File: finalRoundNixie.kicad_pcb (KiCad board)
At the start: 2 copper layers, 37 x 56.3 mm, 60 parts, among them J1 Conn_01x06_Male, J2 HV_IN, J3 Conn_01x06_Female, J4 HV_OUT, Q1 MMBTA42LT1, Q10 MMBTA42LT1, Q11 AO3400, Q12 AO3400, Q13 AO3400, Q14 MMBTA42LT1, Q15 MMBTA42LT1, Q2 MMBTA42LT1, Q3 MMBTA42LT1, Q4 MMBTA42LT1, Q5 MMBTA42LT1, Q6 MMBTA42LT1, Q7 MMBTA42LT1, Q8 MMBTA42LT1, Q9 MMBTA42LT1, U1 74HC595D, U2 nixie-tube-qs27, U3 74HC595D, U4 ams1117-5.0

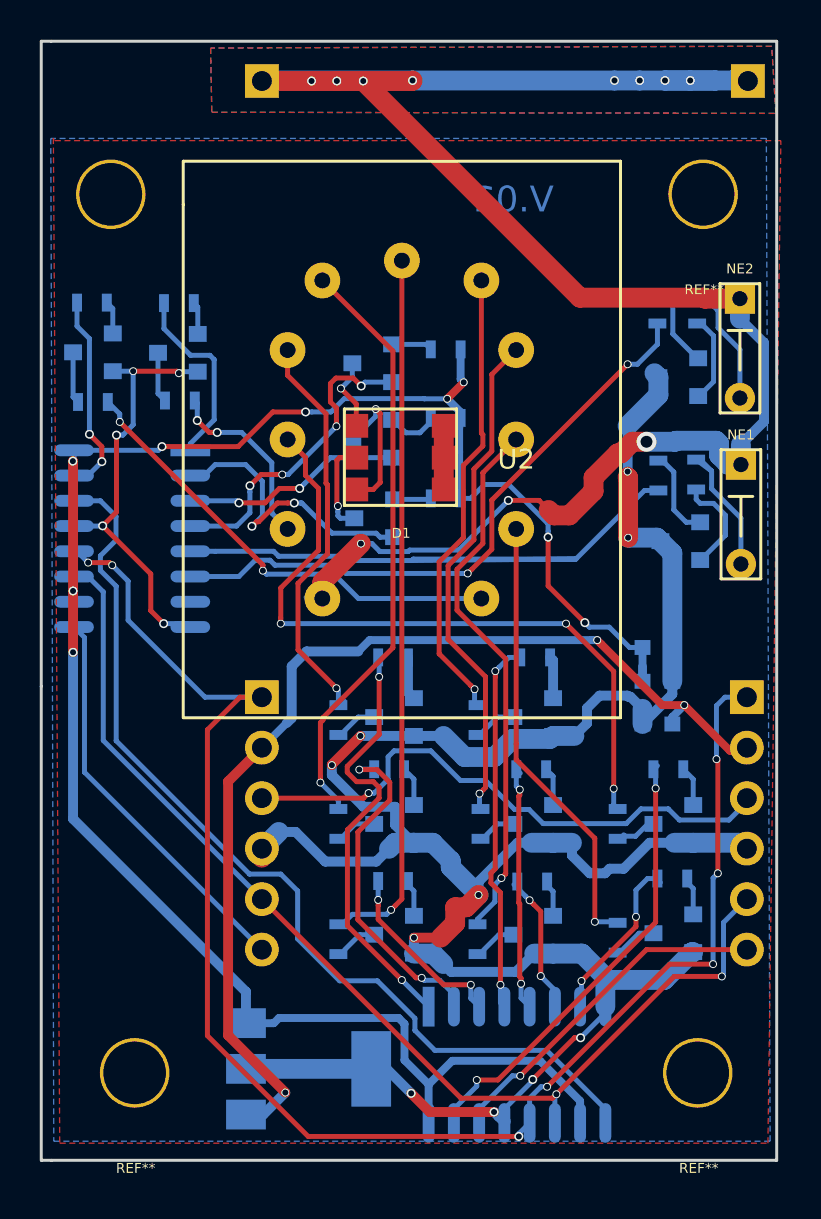
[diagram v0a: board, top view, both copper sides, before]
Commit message: routed qs27-1 on the main pcbnew
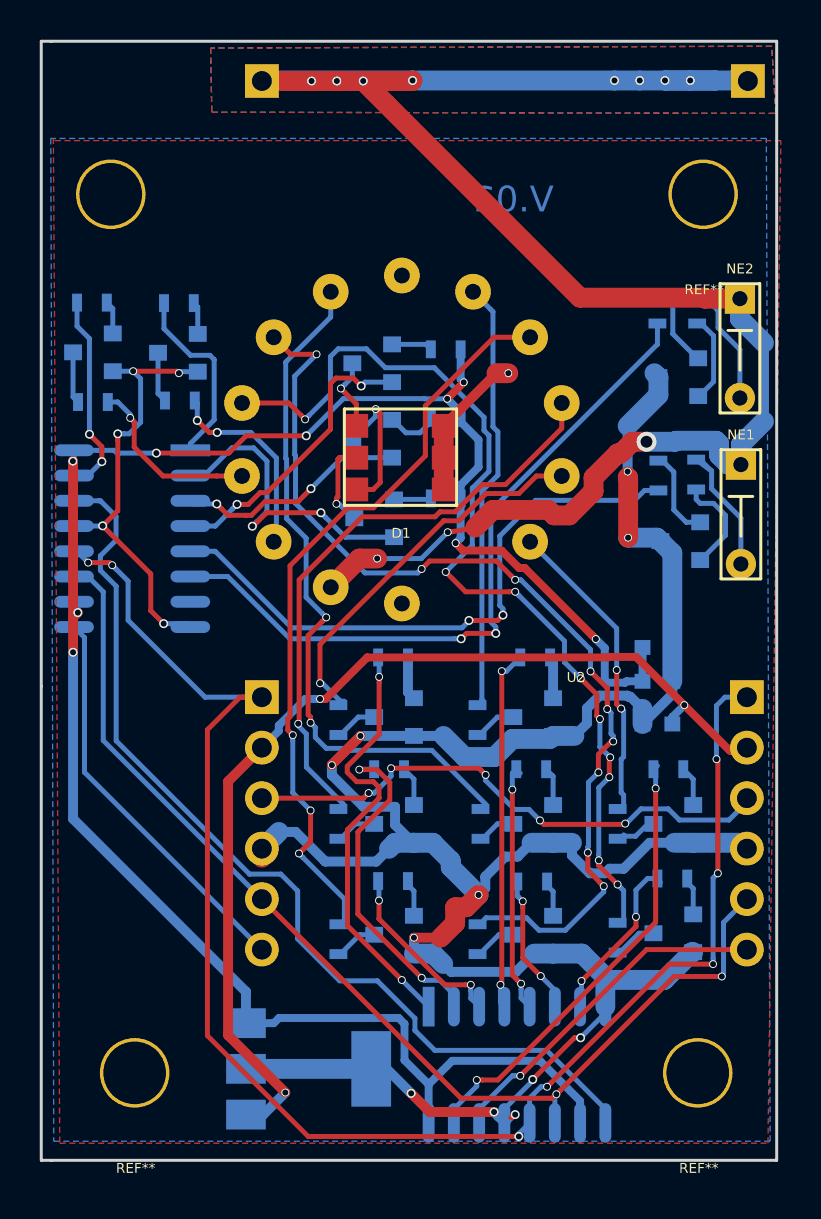
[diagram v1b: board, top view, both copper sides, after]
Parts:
- U2: value nixie-tube-qs27 -> nixie-tube; footprint nixie-tube-fp:qs27-1 -> nixie-tube-fp:qs30-1
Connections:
- U2 pad 1: Net-(J2-Pad1) -> Net-(R10-Pad1)
- U2 pad 2: Net-(R1-Pad1) -> Net-(R9-Pad1)
- U2 pad 3: Net-(R10-Pad1) -> Net-(R8-Pad1)
- U2 pad 4: Net-(R9-Pad1) -> Net-(R7-Pad1)
- U2 pad 5: Net-(R8-Pad1) -> Net-(R6-Pad1)
- U2 pad 6: Net-(R7-Pad1) -> Net-(R5-Pad1)
- U2 pad 7: Net-(R6-Pad1) -> Net-(R4-Pad1)
- U2 pad 8: Net-(R5-Pad1) -> Net-(R3-Pad1)
- U2 pad 9: Net-(R4-Pad1) -> Net-(R2-Pad1)
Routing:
- net Net-(R3-Pad1): track 22.6 -> 48.4 mm, vias 1 -> 9
- net Net-(R4-Pad1): track 27.2 -> 49.6 mm, vias 1 -> 9
- net Net-(R10-Pad1): track 35.4 -> 15.3 mm, vias 3 -> 2
- net Net-(R2-Pad1): track 23.5 -> 9.34 mm, vias 2 -> 1
- net Net-(R5-Pad1): track 25.4 -> 34.7 mm, vias 1 -> 2
- net GND: track 149.0 -> 154.6 mm, vias 15 -> 17
- net /DotD: track 31.5 -> 36.0 mm
- net Net-(J2-Pad1): track 95.4 -> 92.0 mm
- net /DotU: track 33.5 -> 30.6 mm, vias 0 -> 2
- net +VDC: track 53.7 -> 51.6 mm
- net Net-(R7-Pad1): track 35.8 -> 37.9 mm, vias 1 -> 3
- net /Red: track 15.1 -> 16.3 mm
- net /Blue: track 16.1 -> 15.0 mm, vias 4 -> 2
- net Net-(R9-Pad1): track 20.4 -> 19.2 mm
- net Net-(R6-Pad1): track 23.1 -> 22.2 mm, vias 1 -> 0
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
